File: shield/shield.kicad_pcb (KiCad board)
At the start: 2 copper layers, 25.7 x 34.4 mm, 3 parts, among them P1 CONN_01X08, P2 CONN_01X08

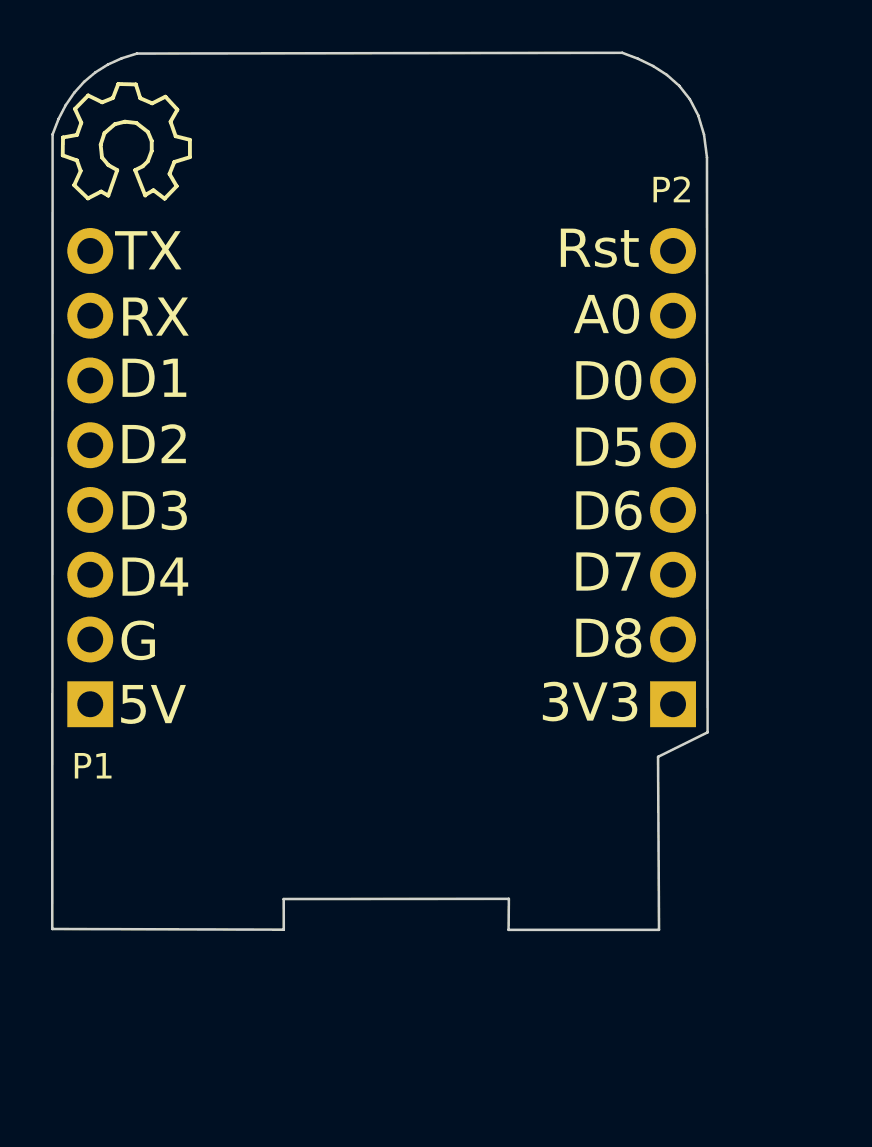
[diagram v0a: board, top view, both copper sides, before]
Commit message: Schematic changes as per merge request discussion, and beginning PCB layout
Changes:
* Schematic
 * Changed rotary encoder schematic part
 * Added debounce circuitry to all rotary encoder signal lines
 * Changed rotary encoder pinout to match existing circuitry
 * Changed MOSFETs to GSD style
 * Added footprints for all components (ensuring hand solderability of all components)
* Library
 * Added custom footprints library for modified footprints / additional ones required
 * Added '3d' folder for attaching 3D bodies to components
* PCB
 * Initial placement of PCB completed
 * Removed pin names from bottom side silk screen
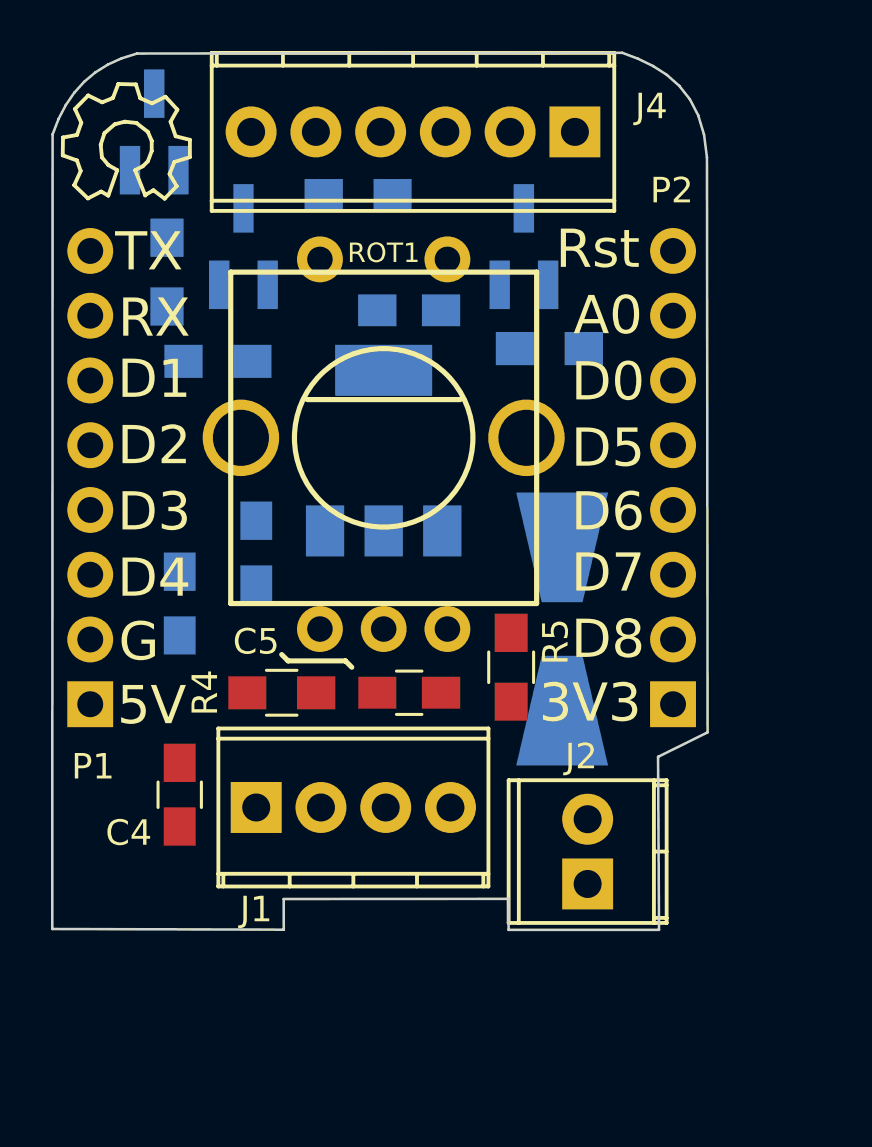
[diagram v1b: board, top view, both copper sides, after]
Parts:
- added C1: 10uF, Capacitors_SMD:C_0805_HandSoldering, B.Cu at (134.0, 98.0)
- added C2: 100nF, Capacitors_SMD:C_0805_HandSoldering, B.Cu at (131.0, 100.0)
- added C3: 22uF, Capacitors_SMD:C_0805_HandSoldering, B.Cu at (140.0, 88.5)
- added C4: 100nF, Capacitors_SMD:C_0805_HandSoldering, F.Cu at (131.0, 107.5)
- added C5: 100nF, Capacitors_SMD:C_0805_HandSoldering, F.Cu at (140.0, 103.5)
- added D1: D, custom_footprints:D_SMB-SMC_Universal_Handsoldering, B.Cu at (146.0, 101.0)
- added J1: Screw_Terminal_1x04, Connectors_Terminal_Blocks:TerminalBlock_Pheonix_MPT-2.54mm_4pol, F.Cu at (134.0, 108.0)
- added J2: Screw_Terminal_1x02, Connectors_Terminal_Blocks:TerminalBlock_Pheonix_MPT-2.54mm_2pol, F.Cu at (147.0, 111.0)
- added J4: Screw_Terminal_1x06, Connectors_Terminal_Blocks:TerminalBlock_Pheonix_MPT-2.54mm_6pol, F.Cu at (146.5, 81.5)
- added Q1: Q_NMOS_GSD, custom_footprints:SOT-23_Handsoldering, B.Cu at (144.5, 86.0)
- added Q2: Q_NMOS_GSD, custom_footprints:SOT-23_Handsoldering, B.Cu at (133.5, 86.0)
- added Q3: Q_NMOS_GSD, custom_footprints:SOT-23_Handsoldering, B.Cu at (130.0, 81.5)
- added R1: 220R, Resistors_SMD:R_0805_HandSoldering, B.Cu at (145.5, 90.0)
- added R2: 220R, Resistors_SMD:R_0805_HandSoldering, B.Cu at (132.5, 90.5)
- added R3: 220R, Resistors_SMD:R_0805_HandSoldering, B.Cu at (130.5, 87.0)
- added R4: 27k, Resistors_SMD:R_0805_HandSoldering, F.Cu at (135.0, 103.5)
- added R5: 27k, Resistors_SMD:R_0805_HandSoldering, F.Cu at (144.0, 102.5)
- added R6: 27k, Resistors_SMD:R_0805_HandSoldering, B.Cu at (138.0, 84.0)
- added ROT1: ROTARY-ENCODER, custom_footprints:SF-ROTARY-ENCODER, F.Cu at (139.0, 93.5)
- added U1: LM1117-3.3, SOT-223, B.Cu at (139.0, 94.0)
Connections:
- P1 pad 2: /GND -> GND
- P1 pad 3: /D4 -> /MCU_SWITCH
- P1 pad 4: /D3 -> /PIR_IN
- P1 pad 5: /D2 -> /MCU_B
- P1 pad 6: /D1 -> /MCU_A
- P2 pad 1: /+3.3V -> +3V3
- P2 pad 2: /D8 -> /D_OUT
- P2 pad 3: /D7 -> /LED_DRIVE_1
- P2 pad 4: /D6 -> /LED_DRIVE_2
- P2 pad 5: /D5 -> /LED_DRIVE_3

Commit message: Updated PCB to have rotary encoder on top side of PCB and terminal blocks on bottom of PCB. PCB outline slightly adjusted to allow for large components (now overhangs the incuts on the Wemos board for reset switch and USB connector).
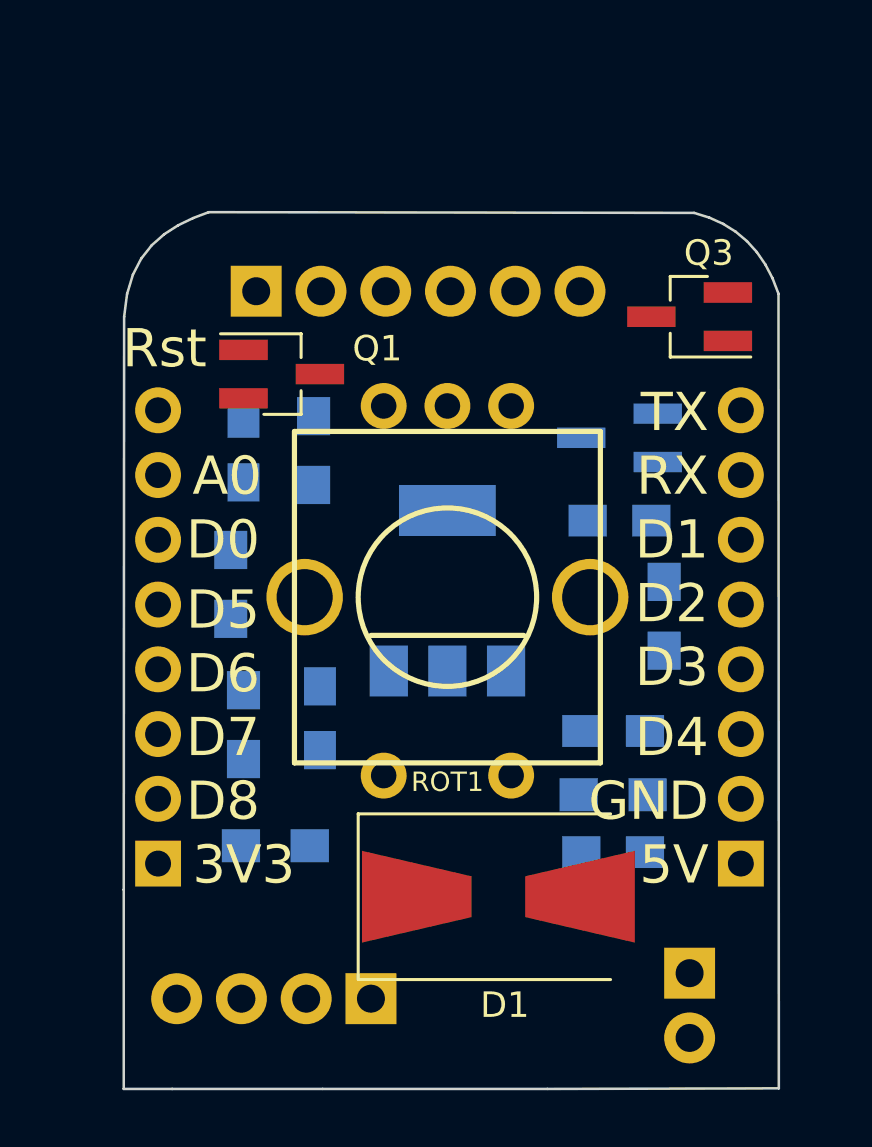
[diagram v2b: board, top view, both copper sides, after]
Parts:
- ?, C4, C5, J1, J2, J4, P1, P2, R4, R5: moved to B.Cu
- D1, Q1, Q3: moved to F.Cu
- moved P1 26.3 mm to (153.0, 110.2), turned to 0 degrees
- moved R6 25.5 mm to (148.0, 107.5), turned to 180 degrees
- moved ? 23.2 mm to (151.2, 88.5), turned to 180 degrees
- moved Q3 22.2 mm to (151.0, 88.8), turned to 180 degrees
- moved P2 21.1 mm to (130.2, 110.2), turned to 0 degrees
- moved C2 19.6 mm to (148.0, 109.8), turned to 180 degrees
- moved R2 19.1 mm to (134.8, 109.5)
- moved R1 19.0 mm to (133.5, 104.8), turned to 90 degrees
- moved C4 17.2 mm to (148.0, 105.0), turned to 180 degrees
- moved Q2 16.5 mm to (148.2, 93.5), turned to 180 degrees
- moved R4 15.3 mm to (150.0, 100.5), turned to 270 degrees
- moved J4 14.0 mm to (134.0, 87.8), turned to 0 degrees
- moved R3 12.5 mm to (133.0, 99.2)
- moved C3 11.7 mm to (148.2, 96.8)
- moved C5 11.5 mm to (133.5, 94.0), turned to 90 degrees
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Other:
- outline, holes or cut-outs redrawn
- board text added: "GND"
- board text removed: "G"

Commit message: Rotated J1 to face bottom edge, and brought J1 and J2 closer to centre of PCB
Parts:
- moved J1 2.75 mm to (141.2, 115.5)
- moved J2 1.80 mm to (149.5, 115.5), turned to 180 degrees
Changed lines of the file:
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@@
   )
   (module Connectors_Terminal_Blocks:TerminalBlock_Pheonix_MPT-2.54mm_4pol (layer B.Cu)
-    (at 138.5 115.5 180)
+    (at 141.25 115.5 180)
     (descr "4-way 2.54mm pitch terminal block, Phoenix MPT series")
-    (fp_text reference J1 (at -2.5 -2.75 180) (layer B.SilkS)
+    (fp_text reference J1 (at 10.5 -2.75 180) (layer B.SilkS)
       (effects (font (size 1 1) (thickness 0.15)) (justify mirror))
     )
@@
   )
   (module Connectors_Terminal_Blocks:TerminalBlock_Pheonix_MPT-2.54mm_2pol (layer B.Cu)
-    (at 151 114.5 270)
+    (at 149.5 115.5 180)
     (descr "2-way 2.54mm pitch terminal block, Phoenix MPT series")
-    (fp_text reference J2 (at 2.25 4.25 540) (layer B.SilkS)
-      (effects (font (size 1 1) (thickness 0.15)) (justify mirror))
-    )
-    (fp_text value Screw_Terminal_1x02 (at 1.27 -4.50088 270) (layer B.Fab)
+    (fp_text reference J2 (at -2.75 -2.75 180) (layer B.SilkS)
+      (effects (font (size 1 1) (thickness 0.15)) (justify mirror))
+    )
+    (fp_text value Screw_Terminal_1x02 (at 1.27 -4.50088 180) (layer B.Fab)
       (effects (font (size 1 1) (thickness 0.15)) (justify mirror))
     )
@@
     (fp_line (start 4.06908 3.0988) (end -1.52908 3.0988) (layer B.SilkS) (width 0.15))
     (fp_line (start -1.52908 3.0988) (end -1.52908 -3.0988) (layer B.SilkS) (width 0.15))
-    (pad 2 thru_hole oval (at 2.54 0 270) (size 1.99898 1.99898) (drill 1.09728) (layers *.Cu *.Mask)
-      (net 8 GND))
-    (pad 1 thru_hole rect (at 0 0 270) (size 1.99898 1.99898) (drill 1.09728) (layers *.Cu *.Mask)
+    (pad 2 thru_hole oval (at 2.54 0 180) (size 1.99898 1.99898) (drill 1.09728) (layers *.Cu *.Mask)
+      (net 8 GND))
+    (pad 1 thru_hole rect (at 0 0 180) (size 1.99898 1.99898) (drill 1.09728) (layers *.Cu *.Mask)
       (net 11 "Net-(D1-Pad2)"))
     (model Terminal_Blocks.3dshapes/TerminalBlock_Pheonix_MPT-2.54mm_2pol.wrl
@@
     (tags "Diode Universal SMB SMC Handsoldering ")
     (attr smd)
-    (fp_text reference D1 (at 0.25 4.25) (layer F.SilkS)
+    (fp_text reference D1 (at -6.75 2) (layer F.SilkS)
       (effects (font (size 1 1) (thickness 0.15)))
     )

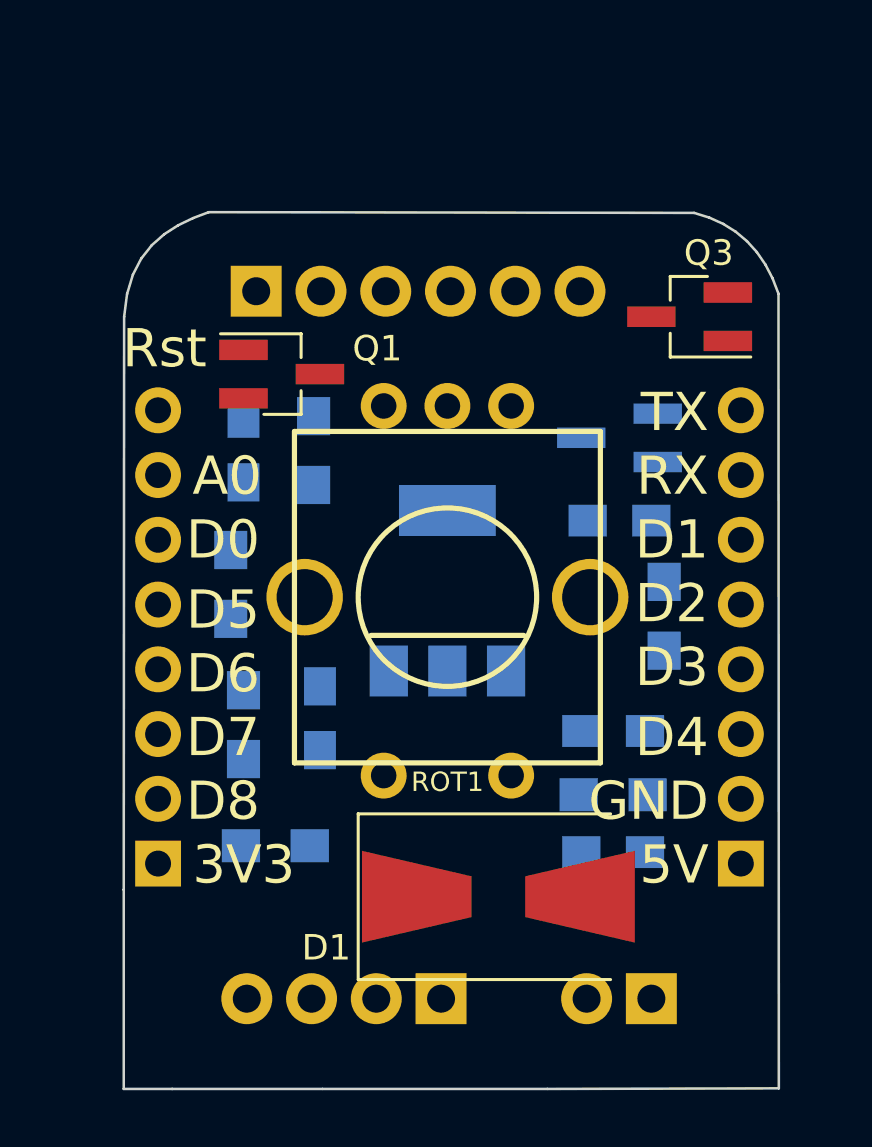
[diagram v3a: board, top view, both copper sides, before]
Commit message: Routed PCB, and added a filled-out BOM (Digi-Key source)
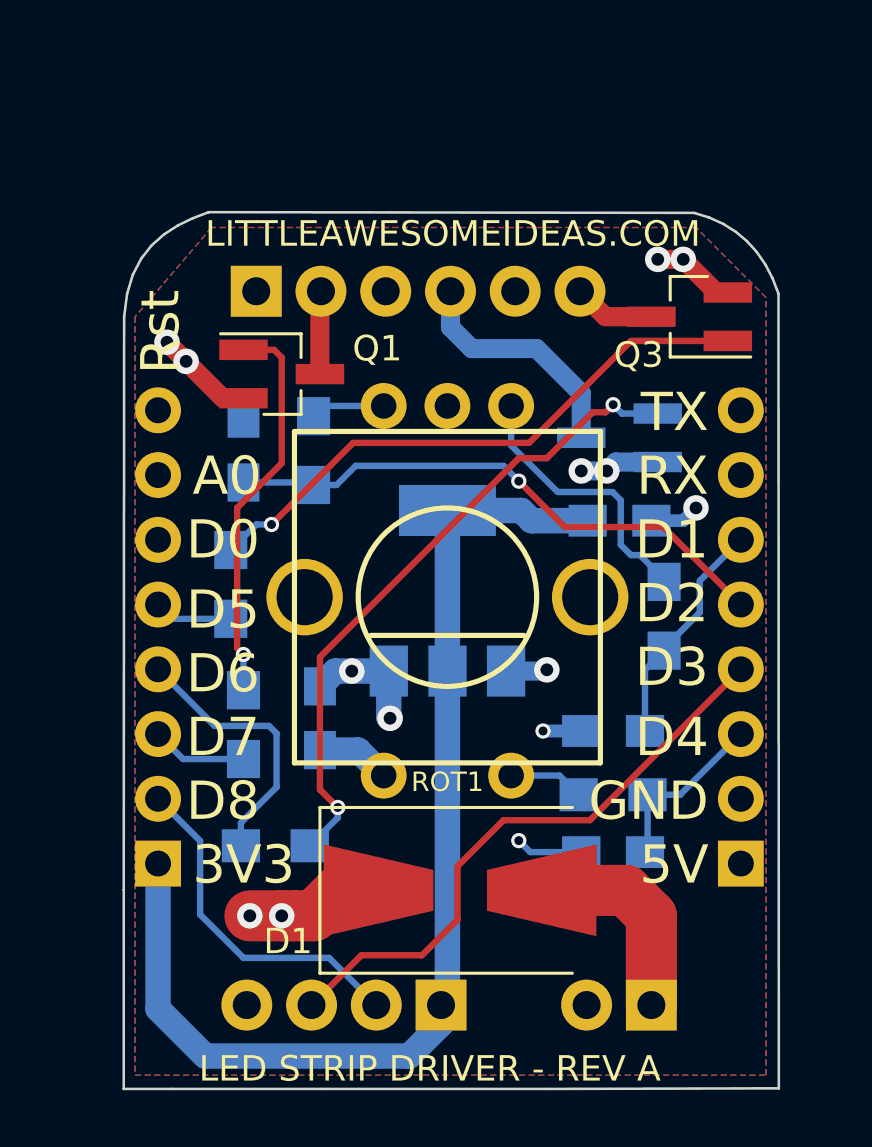
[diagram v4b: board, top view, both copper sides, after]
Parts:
- moved D1 1.52 mm to (142.0, 111.2)
- moved J1 0.25 mm to (141.2, 115.8)
- moved J2 0.25 mm to (149.5, 115.8)
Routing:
- net +3V3: track 0.00 -> 44.0 mm
- net Net-(Q2-Pad1): track 0.00 -> 25.6 mm, vias 0 -> 2
- net GND: track 0.00 -> 24.2 mm, vias 0 -> 10
- net /PIR_IN: track 0.00 -> 23.5 mm
- net Net-(Q3-Pad1): track 0.00 -> 22.9 mm, vias 0 -> 1
- net /MCU_B: track 0.00 -> 22.1 mm, vias 0 -> 1
- net Net-(Q1-Pad1): track 0.00 -> 15.5 mm, vias 0 -> 1
- net /D_OUT: track 0.00 -> 13.6 mm
- net +12V: track 0.00 -> 11.3 mm, vias 0 -> 4
- net /ENC_A: track 0.00 -> 10.8 mm
- net /LED_DRIVE_2: track 0.00 -> 10.7 mm
- net Net-(J4-Pad4): track 0.00 -> 9.36 mm
- net /MCU_A: track 0.00 -> 9.06 mm
- net Net-(D1-Pad2): track 0.00 -> 8.21 mm
- net /MCU_SWITCH: track 0.00 -> 6.94 mm
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- added copper zone on In2.Cu, net +12V
- added copper zone on B.Cu, net GND
- added copper zone on F.Cu, net GND
- added copper zone on In1.Cu, net GND
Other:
- copper layers 2 -> 4
- net class Default: via_drill 0.4 -> 0.35
- net class Power added: clearance 0.2, trace_width 0.5, via_dia 0.6, via_drill 0.35
- rule trace_min: 0.2 -> 0.1
- board text added: "LED STRIP DRIVER - REV A"
- board text added: "LITTLEAWESOMEIDEAS.COM"

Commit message: Updated PCB to 2 layers - WIP
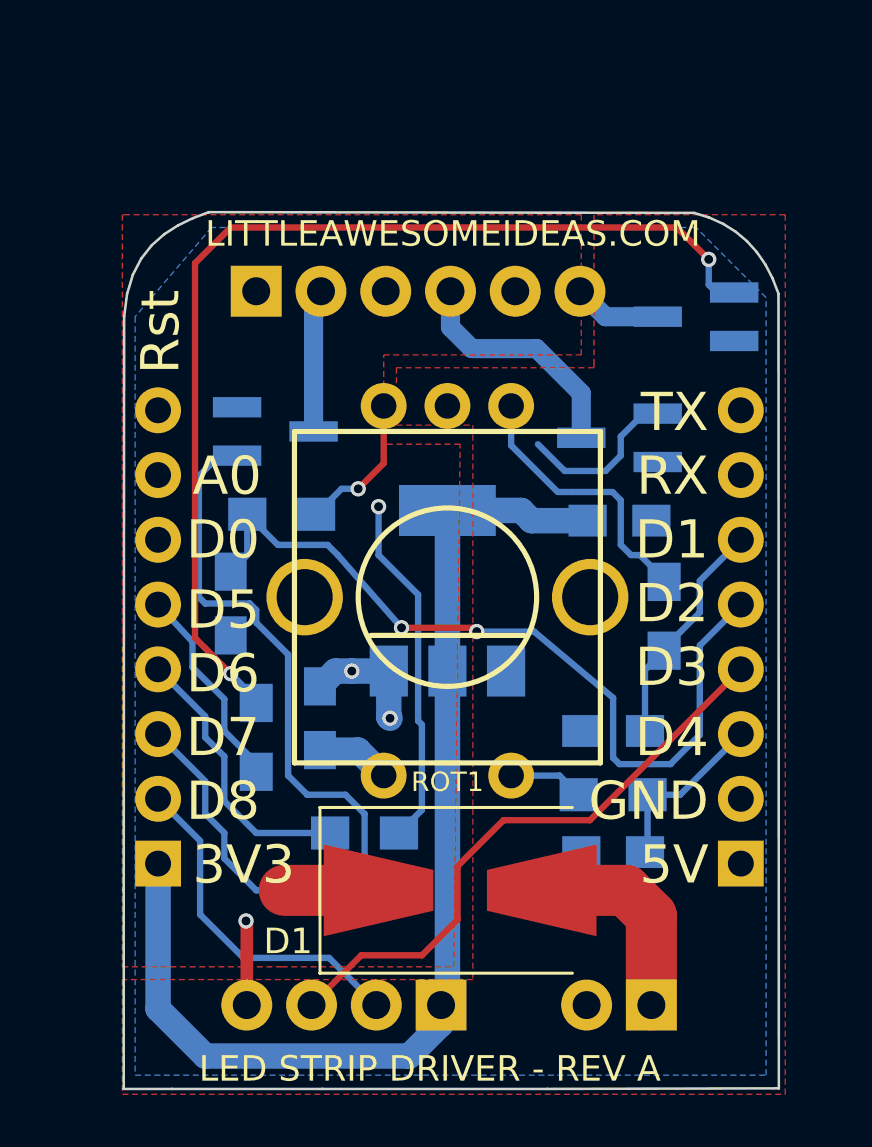
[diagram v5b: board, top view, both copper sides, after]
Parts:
- Q1, Q3: moved to B.Cu
- moved R1 8.05 mm to (138.2, 111.2), turned to 0 degrees
- moved R3 6.08 mm to (134.0, 105.2)
- moved C5 6.02 mm to (133.0, 100.0), turned to 270 degrees
- moved R2 3.54 mm to (138.2, 109.0)
- moved R5 2.80 mm to (135.0, 96.5), turned to 180 degrees
- moved Q1 2.26 mm to (134.8, 93.2)
- moved Q3 0.25 mm to (151.2, 88.8)
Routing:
- net Net-(Q3-Pad1): track 22.9 -> 41.6 mm, vias 1 -> 2
- net GND: track 24.2 -> 6.23 mm, vias 10 -> 1
- net /MCU_B: track 22.1 -> 31.9 mm, vias 1 -> 2
- net Net-(Q1-Pad1): track 15.5 -> 23.2 mm, vias 1 -> 0
- net /LED_DRIVE_1: track 3.76 -> 10.6 mm
- net /LED_DRIVE_3: track 3.08 -> 8.92 mm
- net Net-(Q2-Pad1): track 25.6 -> 20.4 mm, vias 2 -> 1
- net /ENC_B: track 2.92 -> 5.73 mm, vias 0 -> 1
- net Net-(J4-Pad2): track 3.27 -> 5.62 mm
- net +12V: track 11.3 -> 9.59 mm, vias 4 -> 2
- added copper zone on F.Cu, net +12V
- removed copper zone on In2.Cu, net +12V
- removed copper zone on In1.Cu, net GND
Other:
- copper layers 4 -> 2
